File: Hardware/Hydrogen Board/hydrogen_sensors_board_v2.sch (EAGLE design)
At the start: 39 parts, among them U1 ATMEGA328P_TQFP, Y1 16MHz

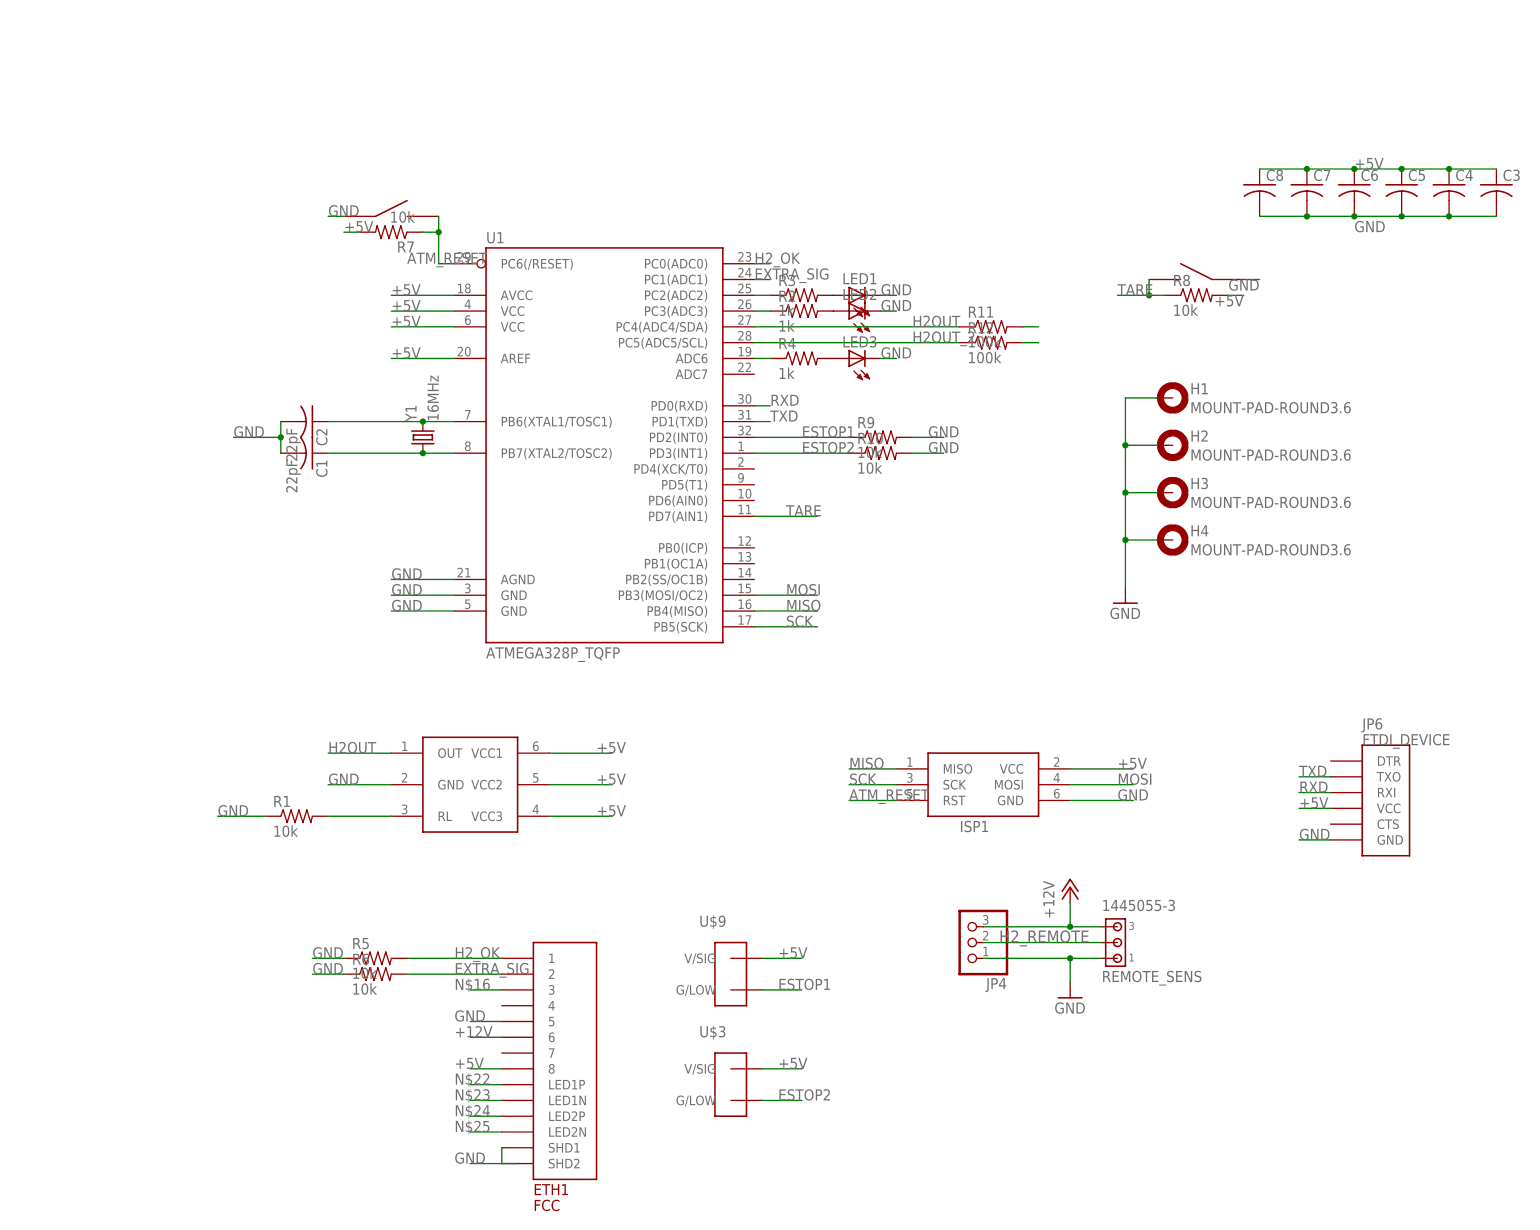
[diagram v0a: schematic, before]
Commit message: more general clean up. Moved LEDs to top layer. Removed some useless traces. Fixed warnings
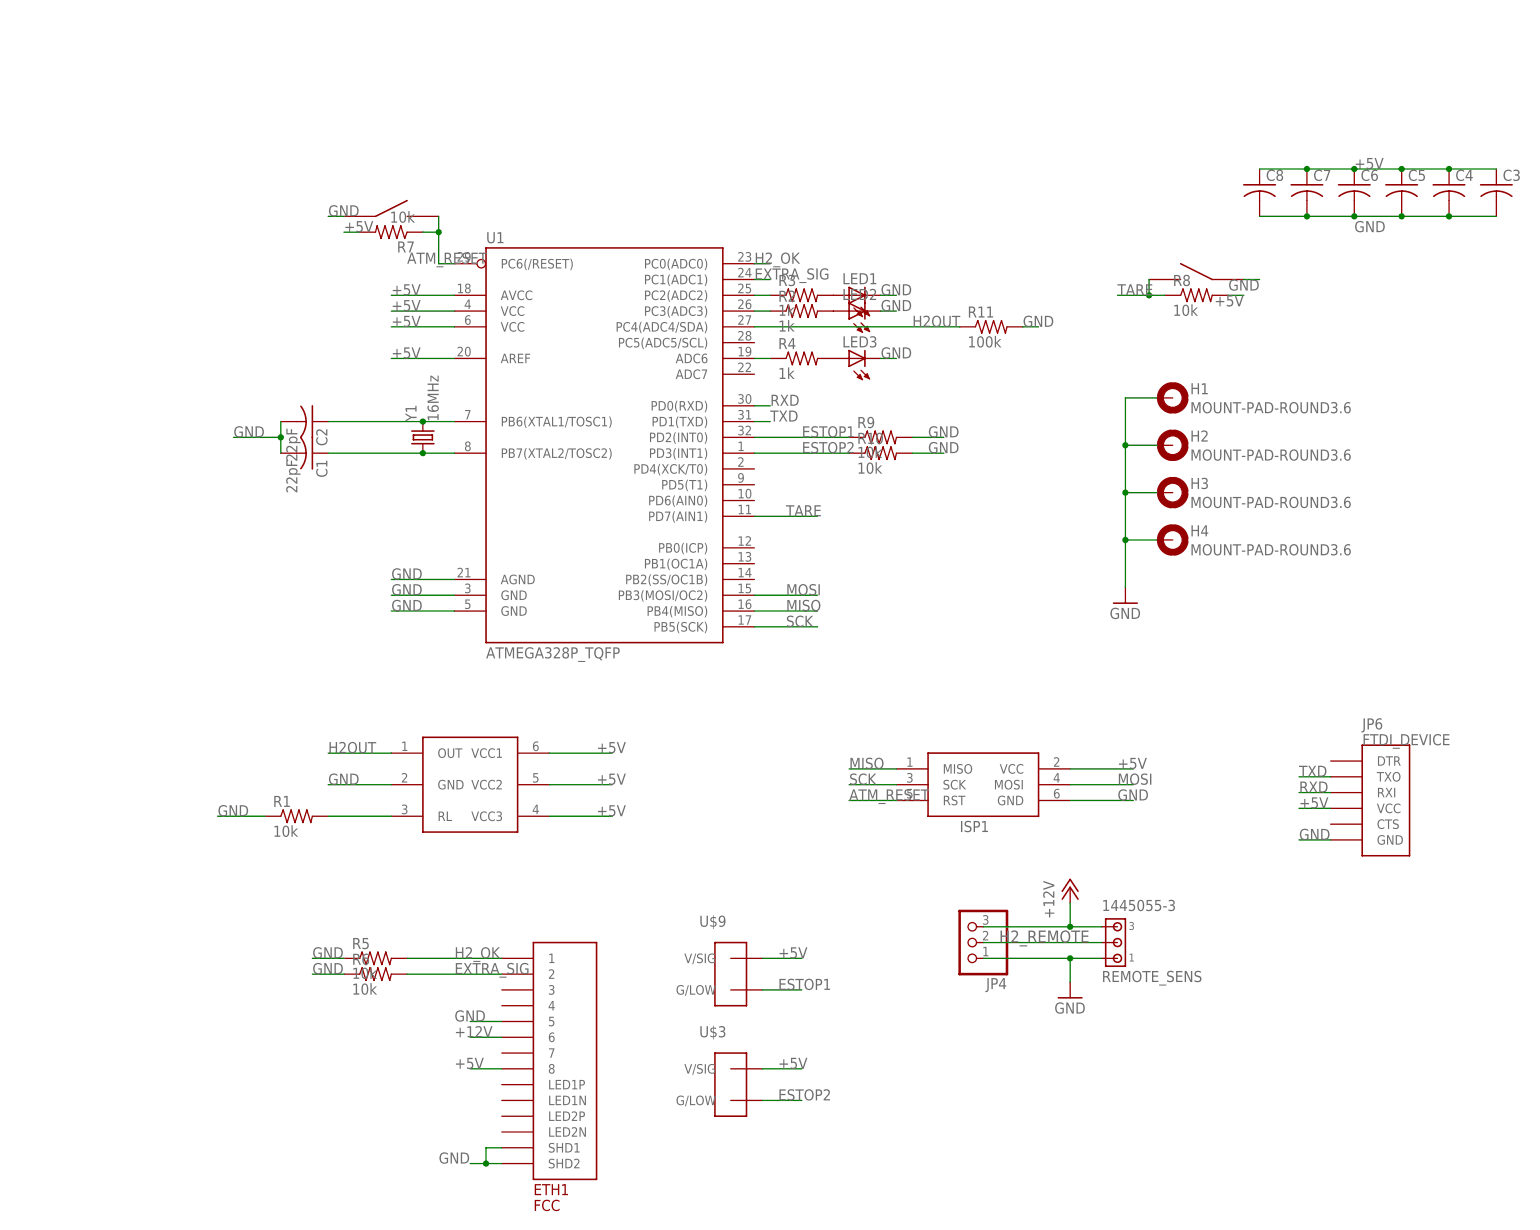
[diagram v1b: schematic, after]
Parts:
- removed R12: 100k, SparkFun-Resistors:RESISTOR0603-RES
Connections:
- removed net H2OUT_2: R12.1, U1.PC5(ADC5/SCL)
- removed net N$10: ETH1.SHD1, ETH1.SHD2
- removed net N$16: ETH1.3
- removed net N$22: ETH1.LED1P
- removed net N$23: ETH1.LED1N
- removed net N$24: ETH1.LED2P
- removed net N$25: ETH1.LED2N
- net GND: now also ETH1.SHD1, ETH1.SHD2; no longer R12.2
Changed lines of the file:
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@@
 <?xml version="1.0" encoding="utf-8"?>
 <!DOCTYPE eagle SYSTEM "eagle.dtd">
-<eagle version="7.7.0">
+<eagle version="8.3.2">
 <drawing>
 <settings>
 <setting alwaysvectorfont="no"/>
+<setting keepoldvectorfont="yes"/>
 <setting verticaltext="up"/>
 </settings>
@@
 <part name="GND27" library="supply1" deviceset="GND" device=""/>
 <part name="R11" library="SparkFun-Resistors" deviceset="RESISTOR" device="0603-RES" value="100k"/>
-<part name="R12" library="SparkFun-Resistors" deviceset="RESISTOR" device="0603-RES" value="100k"/>
 <part name="C3" library="adafruit" deviceset="C-US" device="C0603"/>
 <part name="C4" library="adafruit" deviceset="C-US" device="C0603"/>
@@
 <instance part="GND27" gate="1" x="193.04" y="44.45"/>
 <instance part="R11" gate="G$1" x="180.34" y="152.4"/>
-<instance part="R12" gate="G$1" x="180.34" y="149.86"/>
 <instance part="C3" gate="G$1" x="261.62" y="175.26"/>
 <instance part="C4" gate="G$1" x="254" y="175.26"/>
@@
 </segment>
 <segment>
-<wire x1="104.14" y1="17.78" x2="96.52" y2="17.78" width="0.1524" layer="91"/>
-<label x="93.98" y="17.78" size="1.778" layer="95"/>
-</segment>
-<segment>
 <pinref part="R11" gate="G$1" pin="2"/>
 <wire x1="185.42" y1="152.4" x2="187.96" y2="152.4" width="0.1524" layer="91"/>
-</segment>
-<segment>
-<pinref part="R12" gate="G$1" pin="2"/>
-<wire x1="185.42" y1="149.86" x2="187.96" y2="149.86" width="0.1524" layer="91"/>
+<label x="185.42" y="152.4" size="1.778" layer="95"/>
 </segment>
 <segment>
@@
 <label x="238.76" y="167.64" size="1.778" layer="95"/>
 </segment>
+<segment>
+<pinref part="ETH1" gate="G$1" pin="SHD1"/>
+<wire x1="101.6" y1="20.32" x2="99.06" y2="20.32" width="0.1524" layer="91"/>
+<wire x1="99.06" y1="20.32" x2="99.06" y2="17.78" width="0.1524" layer="91"/>
+<pinref part="ETH1" gate="G$1" pin="SHD2"/>
+<wire x1="99.06" y1="17.78" x2="101.6" y2="17.78" width="0.1524" layer="91"/>
+<wire x1="99.06" y1="17.78" x2="96.52" y2="17.78" width="0.1524" layer="91"/>
+<junction x="99.06" y="17.78"/>
+<label x="91.44" y="17.78" size="1.778" layer="95"/>
+</segment>
 </net>
 <net name="N$2" class="0">
@@
 </segment>
 </net>
-<net name="N$16" class="0">
-<segment>
-<pinref part="ETH1" gate="G$1" pin="3"/>
-<wire x1="101.6" y1="45.72" x2="96.52" y2="45.72" width="0.1524" layer="91"/>
-<label x="93.98" y="45.72" size="1.778" layer="95"/>
-</segment>
-</net>
-<net name="N$22" class="0">
-<segment>
-<pinref part="ETH1" gate="G$1" pin="LED1P"/>
-<wire x1="101.6" y1="30.48" x2="96.52" y2="30.48" width="0.1524" layer="91"/>
-<label x="93.98" y="30.48" size="1.778" layer="95"/>
-</segment>
-</net>
-<net name="N$23" class="0">
-<segment>
-<pinref part="ETH1" gate="G$1" pin="LED1N"/>
-<wire x1="101.6" y1="27.94" x2="96.52" y2="27.94" width="0.1524" layer="91"/>
-<label x="93.98" y="27.94" size="1.778" layer="95"/>
-</segment>
-</net>
-<net name="N$24" class="0">
-<segment>
-<pinref part="ETH1" gate="G$1" pin="LED2P"/>
-<wire x1="101.6" y1="25.4" x2="96.52" y2="25.4" width="0.1524" layer="91"/>
-<label x="93.98" y="25.4" size="1.778" layer="95"/>
-</segment>
-</net>
-<net name="N$25" class="0">
-<segment>
-<pinref part="ETH1" gate="G$1" pin="LED2N"/>
-<wire x1="101.6" y1="22.86" x2="96.52" y2="22.86" width="0.1524" layer="91"/>
-<label x="93.98" y="22.86" size="1.778" layer="95"/>
-</segment>
-</net>
 <net name="RXD" class="0">
 <segment>
@@
 <wire x1="234.95" y1="80.01" x2="229.87" y2="80.01" width="0.1524" layer="91"/>
 <label x="229.87" y="80.01" size="1.778" layer="95"/>
-</segment>
-</net>
-<net name="H2OUT_2" class="0">
-<segment>
-<pinref part="U1" gate="U$1" pin="PC5(ADC5/SCL)"/>
-<wire x1="142.24" y1="149.86" x2="175.26" y2="149.86" width="0.1524" layer="91"/>
-<label x="167.64" y="149.86" size="1.778" layer="95"/>
-<pinref part="R12" gate="G$1" pin="1"/>
 </segment>
 </net>
@@
 </segment>
 </net>
-<net name="N$10" class="0">
-<segment>
-<pinref part="ETH1" gate="G$1" pin="SHD1"/>
-<pinref part="ETH1" gate="G$1" pin="SHD2"/>
-<wire x1="101.6" y1="20.32" x2="101.6" y2="17.78" width="0.1524" layer="91"/>
-</segment>
-</net>

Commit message: added 3.3V LDO (chip and all digital signals are all 3.3V now). Added appropriate voltage divider for hydrogen sensor output (with optional cap)
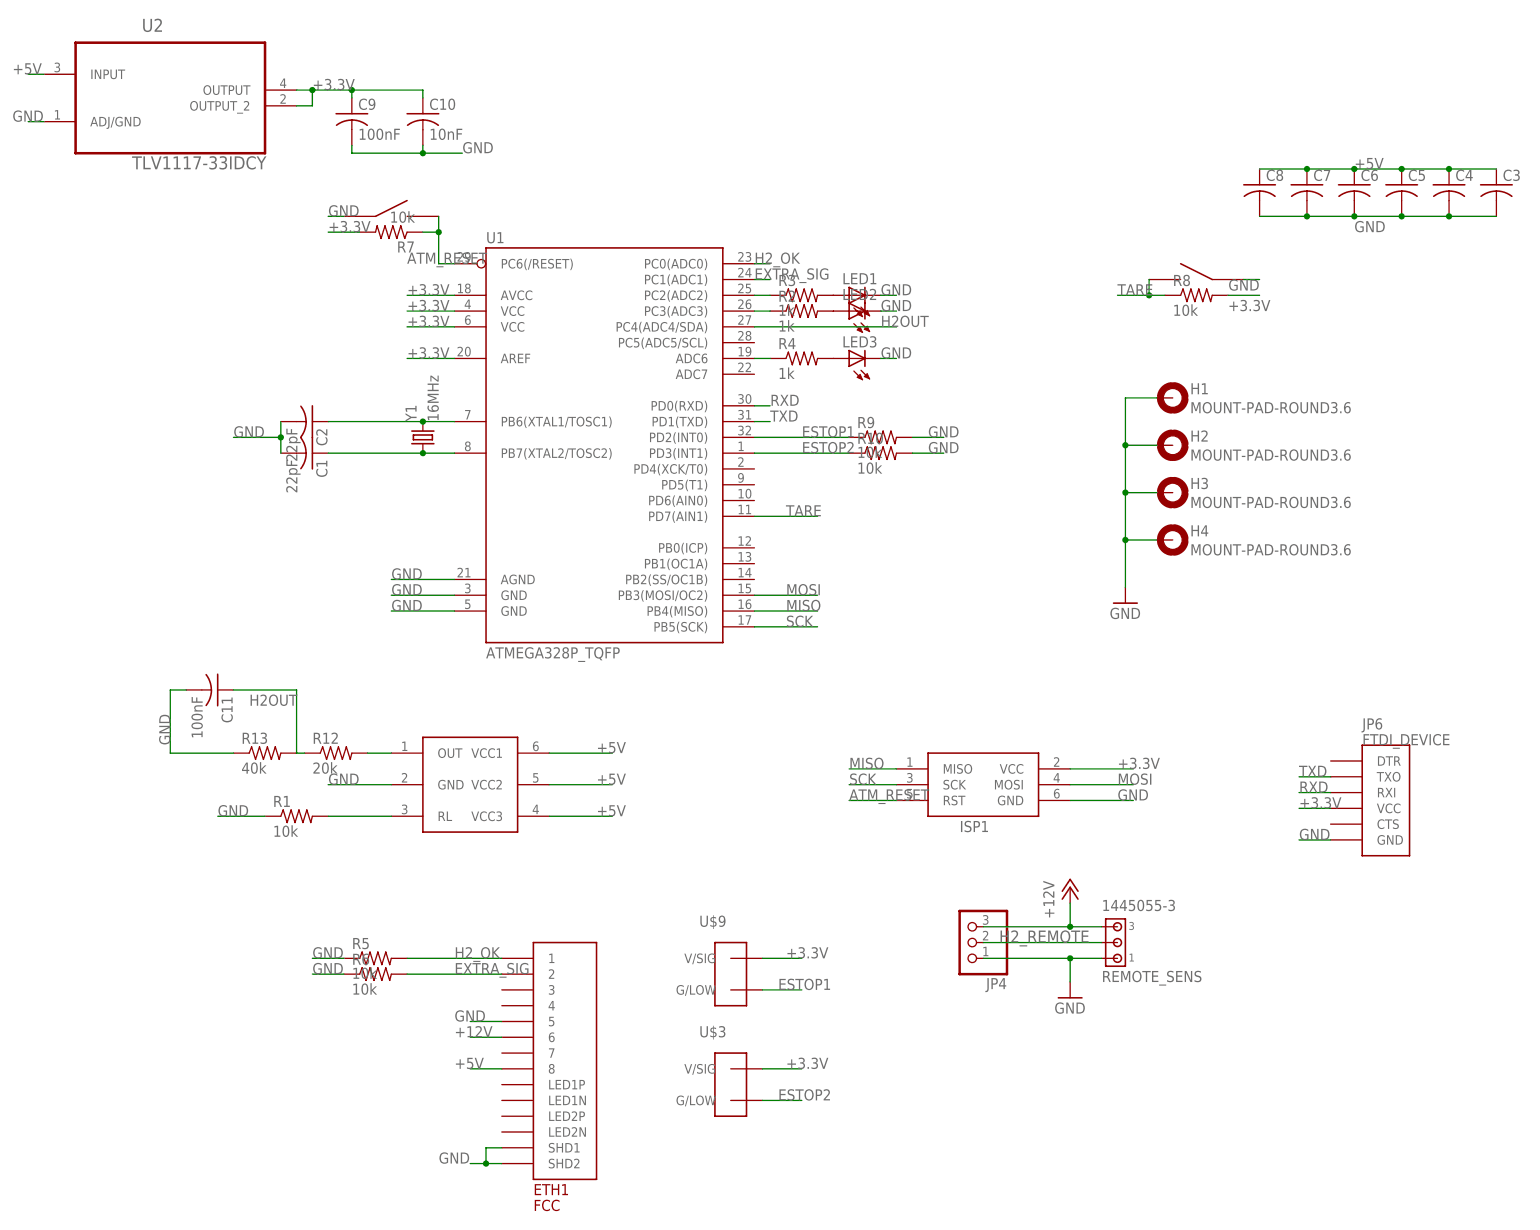
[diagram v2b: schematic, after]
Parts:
- removed R11: 100k, SparkFun-Resistors:RESISTOR0603-RES
- added C10: 10nF, adafruit:C-USC0603
- added C11, C9: 100nF, adafruit:C-USC0603
- added R12: 20k, SparkFun-Passives:RESISTOR0603-RES
- added R13: 40k, SparkFun-Passives:RESISTOR0603-RES
- added U2: TLV1117-33IDCY, Texas Instruments_By_element14_Batch_1:TLV1117-33IDCY
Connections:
- new net +3.3V: C10.1, C9.1, ISP1.VCC, JP6.VCC, R7.2, R8.2, U$3.V/SIG, U$9.V/SIG, U1.AREF, U1.AVCC, U1.VCC@4, U1.VCC@6, U2.OUTPUT, U2.OUTPUT_2
- new net N$10: R12.2, U$1.OUT
- net +5V: now also U2.INPUT; no longer ISP1.VCC, JP6.VCC, R7.2, R8.2, U$3.V/SIG, U$9.V/SIG, U1.AREF, U1.AVCC, U1.VCC@4, U1.VCC@6
- net GND: now also C10.2, C11.2, C9.2, R13.1, U2.ADJ/GND; no longer R11.2
- net H2OUT: now also C11.1, R12.1, R13.2; no longer R11.1, U$1.OUT
